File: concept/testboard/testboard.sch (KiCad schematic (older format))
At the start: 0 parts

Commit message: started design of testboard
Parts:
- added C? (x2): 100n, symbol Device:C_Small
- added IC?: NCP1117DT33T5G, TO229P990X238-4N, symbol hive:NCP1117DT33T5G
- added J?: Probe connector, symbol Connector:Conn_ARM_JTAG_SWD_10
- added J?: Probe out, symbol Connector:Conn_01x05_Male
- added J?: I2C, symbol Connector:Conn_01x02_Male
- added JP?: 1OE, symbol Device:Jumper_NO_Small
- added JP?: 2OE, symbol Device:Jumper_NO_Small
- added JP?: 5V 1B1, symbol Device:Jumper_NO_Small
- added JP?: 5V 1A1, symbol Device:Jumper_NO_Small
- added JP?: IO in, symbol Device:Jumper_NO_Small
- added R? (x3): 100k, symbol Device:R_Small
- added R? (x2): 4k7, symbol Device:R_Small
- added U?: SN74CB3T16211DGGR, SOP50P810X120-56N, symbol hive:SN74CB3T16211DGGR
- added U?: PCA9535CPW,118, SOP65P640X110-24N, symbol hive:PCA9535CPW,118
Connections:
- new net: J?.10 (~RESET~), U?.24 (2A8)
- new net: J?.2 (SWDIO/TMS), U?.26 (2A10)
- new net: J?.4 (SWDCLK/TCK), U?.25 (2A9)
- new net: J?.6 (SWO/TDO), U?.27 (2A11)
- new net: J?.8 (NC/TDI), U?.28 (2A12)
- new net: J?.1 (Pin_1), U?.10 (1A8)
- new net: J?.2 (Pin_2), U?.11 (1A9)
- new net: J?.3 (Pin_3), U?.12 (1A10)
- new net: J?.4 (Pin_4), U?.13 (1A11)
- new net: J?.5 (Pin_5), U?.14 (1A12)
- new net: JP?.2, U?.2 (1A1)
- new net: U?.29 (2B12), U?.42 (1B12)
- new net: U?.30 (2B11), U?.43 (1B11)
- new net: U?.31 (2B10), U?.44 (1B10)
- new net: U?.32 (2B9), U?.45 (1B9)
- new net: U?.33 (2B8), U?.46 (1B8)
- new net: JP?.1, R?.2, U?.54 (1B1)
- new net: JP?.2, R?.2, U?.14 (IO1_1), U?.55 (2~OE)
- new net: JP?.2, R?.2, U?.13 (IO1_0), U?.56 (1~OE)
- new net: JP?.1, U?.15 (IO1_2)
- new net: J?.2 (Pin_2), R?.1, U?.22 (SCL)
- new net: J?.1 (Pin_1), R?.1, U?.23 (SDA)
- new net +3V3: C?.2, C?.2, IC?.4 (OUT_TAB), J?.1 (VTref), JP?.2, R?.1, R?.1, R?.2, R?.2, U?.17 (VCC), U?.24 (VDD)
- new net +5V: IC?.3 (IN), JP?.1, JP?.2
- new net GND: C?.1, C?.1, IC?.1 (GND), J?.3 (GND), J?.5 (GND), J?.9 (GNDDetect), JP?.1, JP?.1, R?.1, U?.1 (~INT), U?.12 (VSS), U?.19 (GND_2), U?.38 (GND_3), U?.49 (GND), U?.8 (GND_4)
- no-connect marks 0 -> 1
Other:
- note added: "5V to 3.3V LDO"

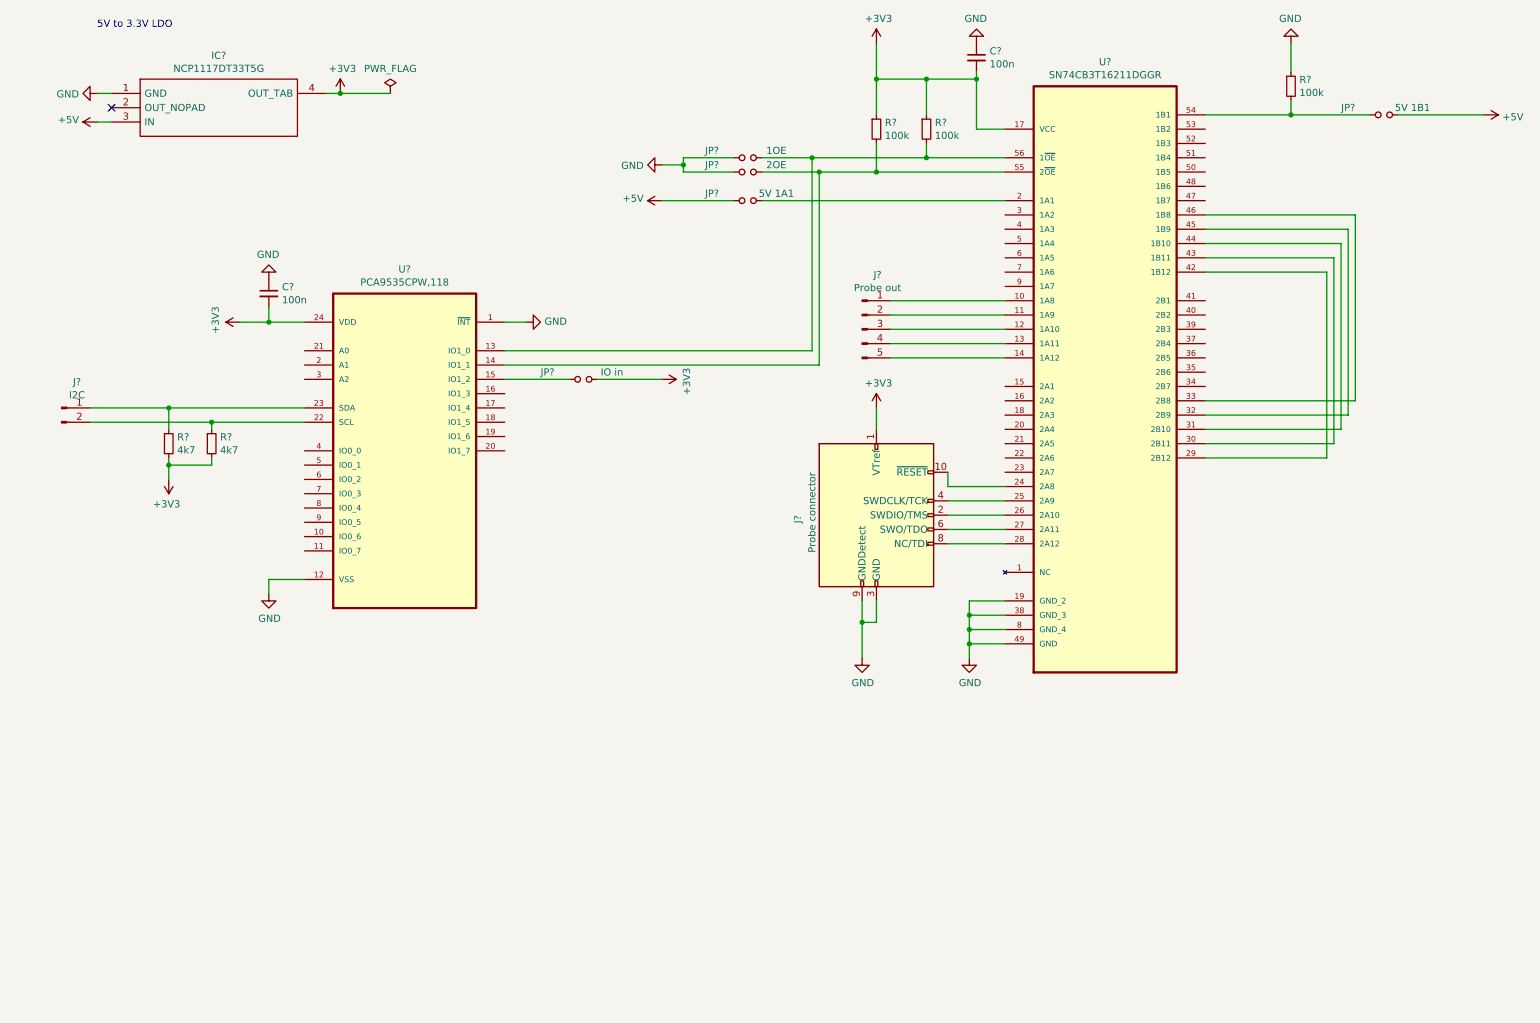
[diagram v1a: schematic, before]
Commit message: finished testboard schematic
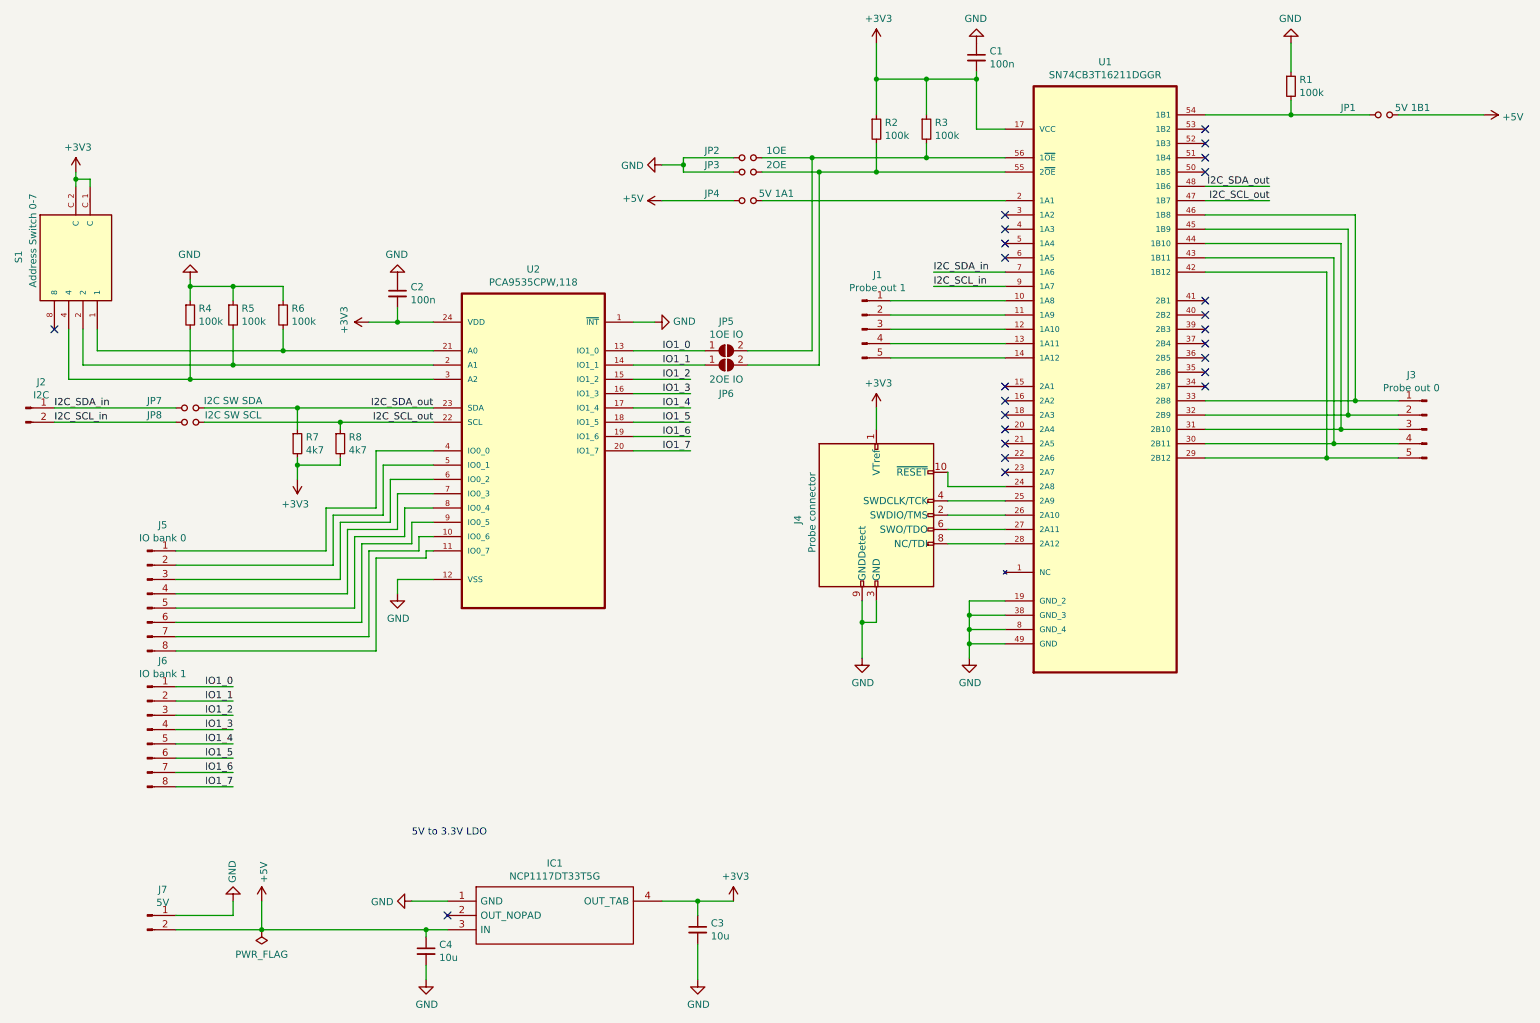
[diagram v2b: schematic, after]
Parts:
- removed JP?: IO in, symbol Device:Jumper_NO_Small
- added C3, C4: 10u, symbol Device:C_Small
- added J3: Probe out 0, symbol Connector:Conn_01x05_Male
- added J5: IO bank 0, symbol Connector:Conn_01x08_Male
- added J6: IO bank 1, symbol Connector:Conn_01x08_Male
- added J7: 5V, symbol Connector:Conn_01x02_Male
- added JP5: 1OE IO, symbol Jumper:SolderJumper_2_Open
- added JP6: 2OE IO, symbol Jumper:SolderJumper_2_Open
- added JP7: I2C SW SDA, symbol Device:Jumper_NO_Small
- added JP8: I2C SW SCL, symbol Device:Jumper_NO_Small
- added R4, R5, R6: 100k, symbol Device:R_Small
- added S1: Address Switch 0-7, SW_RDS-10S-74385-SMT, symbol hive:RDS-10S-74385-SMT
- J1: renamed from J?; value Probe out -> Probe out 1
- gave numbers to parts that had none: 16
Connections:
- net +3V3: now also C3.1, S1.C_1 (C), S1.C_2 (C)
- net +5V: now also C4.1, J7.2 (Pin_2)
- net GND: now also C3.2, C4.2, J7.1 (Pin_1), R4.1, R5.1, R6.1
- net at U1.29 (2B12), U1.42 (1B12): now also J3.5 (Pin_5)
- net at U1.30 (2B11), U1.43 (1B11): now also J3.4 (Pin_4)
- net at U1.31 (2B10), U1.44 (1B10): now also J3.3 (Pin_3)
- net at U1.32 (2B9), U1.45 (1B9): now also J3.2 (Pin_2)
- net at U1.33 (2B8), U1.46 (1B8): now also J3.1 (Pin_1)
- net I2C_SCL_out: now reaches U1.47 (1B7)
- net I2C_SCL_out: now also R8.1, U2.22 (SCL), JP8.2
- net I2C_SDA_out: now reaches U1.48 (1B6)
- net I2C_SDA_out: now also R7.1, U2.23 (SDA), JP7.2
- net at JP3.2, R2.2, U1.55 (2~OE): now also JP6.2 (B); no longer U2.14 (IO1_1)
- net at JP2.2, R3.2, U1.56 (1~OE): now also JP5.2 (B); no longer U2.13 (IO1_0)
- net I2C_SDA_in: now reaches U1.7 (1A6)
- net I2C_SDA_in: now also J2.1 (Pin_1), JP7.1
- net I2C_SCL_in: now reaches U1.9 (1A7)
- net I2C_SCL_in: now also J2.2 (Pin_2), JP8.1
- net at U2.10 (IO0_6): now also J5.7 (Pin_7)
- net at U2.11 (IO0_7): now also J5.8 (Pin_8)
- net IO1_2: now reaches U2.15 (IO1_2)
- net IO1_2: now also J6.3 (Pin_3)
- net IO1_3: now reaches U2.16 (IO1_3)
- net IO1_3: now also J6.4 (Pin_4)
- net IO1_4: now reaches U2.17 (IO1_4)
- net IO1_4: now also J6.5 (Pin_5)
- net IO1_5: now reaches U2.18 (IO1_5)
- net IO1_5: now also J6.6 (Pin_6)
- net IO1_6: now reaches U2.19 (IO1_6)
- net IO1_6: now also J6.7 (Pin_7)
- net at U2.2 (A1): now also R5.2, S1.2
- net IO1_7: now reaches U2.20 (IO1_7)
- net IO1_7: now also J6.8 (Pin_8)
- net at U2.21 (A0): now also R6.2, S1.1
- net at U2.3 (A2): now also R4.2, S1.4
- net at U2.4 (IO0_0): now also J5.1 (Pin_1)
- net at U2.5 (IO0_1): now also J5.2 (Pin_2)
- net at U2.6 (IO0_2): now also J5.3 (Pin_3)
- net at U2.7 (IO0_3): now also J5.4 (Pin_4)
- net at U2.8 (IO0_4): now also J5.5 (Pin_5)
- net at U2.9 (IO0_5): now also J5.6 (Pin_6)
- new net IO1_0: J6.1 (Pin_1), JP5.1 (A), U2.13 (IO1_0)
- new net IO1_1: J6.2 (Pin_2), JP6.1 (A), U2.14 (IO1_1)
- no-connect marks 1 -> 24
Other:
- moved on the sheet: C2, IC1, J2, R7, R8, U2

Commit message: finished testboard layout
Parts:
- removed J4: Probe connector, symbol Connector:Conn_ARM_JTAG_SWD_10
- added J4: probe connector, hive:SAMTEC_FTSH-105-01-F-DV-007, symbol hive:FTSH-105-01-F-DV-007-ARM-10pindebug
- C1, C2: footprint (none) -> Capacitor_SMD:C_0805_2012Metric_Pad1.15x1.40mm_HandSolder
- C3, C4: footprint (none) -> Capacitor_SMD:C_1206_3216Metric_Pad1.42x1.75mm_HandSolder
- IC1: footprint TO229P990X238-4N -> hive:TO229P990X238-4N
- J1, J3: footprint (none) -> Connector_PinHeader_2.54mm:PinHeader_1x05_P2.54mm_Vertical
- J2, J7, JP1, JP2, JP3, JP4: footprint (none) -> Connector_PinHeader_2.54mm:PinHeader_1x02_P2.54mm_Vertical
- J5, J6: footprint (none) -> Connector_PinHeader_2.54mm:PinHeader_1x08_P2.54mm_Vertical
- JP5, JP6, JP7, JP8: footprint (none) -> Jumper:SolderJumper-2_P1.3mm_Open_Pad1.0x1.5mm
- R1, R2, R3, R4, R5, R6, R7, R8: footprint (none) -> Resistor_SMD:R_0805_2012Metric_Pad1.15x1.40mm_HandSolder
- S1: footprint SW_RDS-10S-74385-SMT -> hive:SW_RDS-10S-74385-SMT
- U1: footprint SOP50P810X120-56N -> hive:SOP50P810X120-56N
- U2: footprint SOP65P640X110-24N -> hive:SOP65P640X110-24N
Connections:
- net +3V3: now also J4.01 (VREF)
- net GND: now also J4.03 (GND), J4.05 (GND), J4.09 (GND_detect)
- net at U1.24 (2A8): now also J4.02 (SWDIO/TMS)
- net at U1.26 (2A10): now also J4.06 (SWO/TDO)
- net at U1.25 (2A9): now also J4.04 (SWDCLK/TCK)
- net at U1.27 (2A11): now also J4.08 (NC/TDI)
- net at U1.28 (2A12): now also J4.10 (~RESET~)

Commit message: updated testboard schematics to new symbols
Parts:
- U1: symbol hive:SN74CB3T16211DGGR -> testboard-rescue:SN74CB3T16211DGGR-hive
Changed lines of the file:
@@
 	5600 6900 5350 6900
 $Comp
-L hive:SN74CB3T16211DGGR U1
+L testboard-rescue:SN74CB3T16211DGGR-hive U1
 U 1 1 614CBA49
 P 8200 3100
